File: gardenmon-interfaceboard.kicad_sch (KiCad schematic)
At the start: 0 parts

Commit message: sch: add all connections
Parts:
- added H1, H2, H3, H4: MountingHole, symbol Mechanical:MountingHole
- added J1: Conn_02x20_Odd_Even, symbol Connector_Generic:Conn_02x20_Odd_Even
- added J2, J4, J5: Conn_01x04, symbol Connector_Generic:Conn_01x04
- added J3: Conn_01x10, symbol Connector_Generic:Conn_01x10
- added J6: Conn_01x03, symbol Connector_Generic:Conn_01x03
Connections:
- new net +3.3V: J1.1 (Pin_1), J1.17 (Pin_17)
- new net +3V3: J2.1 (Pin_1), J3.1 (Pin_1), J4.1 (Pin_1), J5.1 (Pin_1), J6.1 (Pin_1)
- new net 1wire_data: J1.7 (Pin_7), J6.2 (Pin_2)
- new net GND: J1.14 (Pin_14), J1.20 (Pin_20), J1.25 (Pin_25), J1.30 (Pin_30), J1.34 (Pin_34), J1.39 (Pin_39), J1.6 (Pin_6), J1.9 (Pin_9), J2.2 (Pin_2), J3.2 (Pin_2), J3.5 (Pin_5), J4.2 (Pin_2), J5.2 (Pin_2), J6.3 (Pin_3)
- new net i2c_scl: J1.5 (Pin_5), J3.3 (Pin_3), J4.3 (Pin_3), J5.3 (Pin_3)
- new net i2c_sda: J1.3 (Pin_3), J3.4 (Pin_4), J4.4 (Pin_4), J5.4 (Pin_4)
- new net smoist_sig: J2.4 (Pin_4), J3.7 (Pin_7)
- no-connect marks 0 -> 32
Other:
- note added: "I2C address 0x23"
- note added: "I2C address 0x40"
- note added: "address pin tied low -> I2C address 0x48"
- note added: "ads1115 ADC"
- note added: "ambient light sensor"
- note added: "ds18b20 temperature sensor module board (module board has built-in pull up for 1wire_data)"
- note added: "raspberry pi zero 2 w header"
- note added: "sht30 temperature/humidity sensor"
- note added: "soil moisture sensor module board"

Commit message: sch/pcb: add footprints, setup PCBNew for OSHPark
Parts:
- H1, H2, H3, H4: footprint (none) -> MountingHole:MountingHole_2.7mm_M2.5
- J1: footprint (none) -> Connector_PinHeader_2.54mm:PinHeader_2x20_P2.54mm_Vertical
- J2, J4, J5: footprint (none) -> Connector_PinHeader_2.54mm:PinHeader_1x04_P2.54mm_Vertical
- J3: footprint (none) -> Connector_PinHeader_2.54mm:PinHeader_1x10_P2.54mm_Vertical
- J6: footprint (none) -> Connector_PinHeader_2.54mm:PinHeader_1x03_P2.54mm_Vertical
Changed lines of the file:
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@@
       (effects (font (size 1.27 1.27)) (justify left) hide)
     )
-    (property "Footprint" "" (at 130.81 59.69 0)
+    (property "Footprint" "Connector_PinHeader_2.54mm:PinHeader_1x04_P2.54mm_Vertical" (at 130.81 59.69 0)
       (effects (font (size 1.27 1.27)) hide)
     )
@@
       (effects (font (size 1.27 1.27)) (justify left) hide)
     )
-    (property "Footprint" "" (at 130.81 91.44 0)
+    (property "Footprint" "Connector_PinHeader_2.54mm:PinHeader_1x04_P2.54mm_Vertical" (at 130.81 91.44 0)
       (effects (font (size 1.27 1.27)) hide)
     )
@@
       (effects (font (size 1.27 1.27)) (justify left) hide)
     )
-    (property "Footprint" "" (at 130.81 123.19 0)
+    (property "Footprint" "Connector_PinHeader_2.54mm:PinHeader_1x04_P2.54mm_Vertical" (at 130.81 123.19 0)
       (effects (font (size 1.27 1.27)) hide)
     )
@@
       (effects (font (size 1.27 1.27)) (justify left))
     )
-    (property "Footprint" "" (at 68.58 149.86 0)
+    (property "Footprint" "MountingHole:MountingHole_2.7mm_M2.5" (at 68.58 149.86 0)
       (effects (font (size 1.27 1.27)) hide)
     )
@@
       (effects (font (size 1.27 1.27)) (justify left))
     )
-    (property "Footprint" "" (at 68.58 144.78 0)
+    (property "Footprint" "MountingHole:MountingHole_2.7mm_M2.5" (at 68.58 144.78 0)
       (effects (font (size 1.27 1.27)) hide)
     )
@@
       (effects (font (size 1.27 1.27)) (justify left) hide)
     )
-    (property "Footprint" "" (at 193.04 124.46 0)
+    (property "Footprint" "Connector_PinHeader_2.54mm:PinHeader_1x03_P2.54mm_Vertical" (at 193.04 124.46 0)
       (effects (font (size 1.27 1.27)) hide)
     )
@@
       (effects (font (size 1.27 1.27)) (justify left))
     )
-    (property "Footprint" "" (at 68.58 160.02 0)
+    (property "Footprint" "MountingHole:MountingHole_2.7mm_M2.5" (at 68.58 160.02 0)
       (effects (font (size 1.27 1.27)) hide)
     )
@@
       (effects (font (size 1.27 1.27)) (justify left) hide)
     )
-    (property "Footprint" "" (at 191.77 67.31 0)
+    (property "Footprint" "Connector_PinHeader_2.54mm:PinHeader_1x10_P2.54mm_Vertical" (at 191.77 67.31 0)
       (effects (font (size 1.27 1.27)) hide)
     )
@@
       (effects (font (size 1.27 1.27)) hide)
     )
-    (property "Footprint" "" (at 76.2 82.55 0)
+    (property "Footprint" "Connector_PinHeader_2.54mm:PinHeader_2x20_P2.54mm_Vertical" (at 76.2 82.55 0)
       (effects (font (size 1.27 1.27)) hide)
     )
@@
       (effects (font (size 1.27 1.27)) (justify left))
     )
-    (property "Footprint" "" (at 68.58 154.94 0)
-      (effects (font (size 1.27 1.27)) hide)
-    )
+    (property "Footprint" "MountingHole:MountingHole_2.7mm_M2.5" (at 68.58 154.94 0)
+      (effects (font (size 1.27 1.27)) hide)
+    )

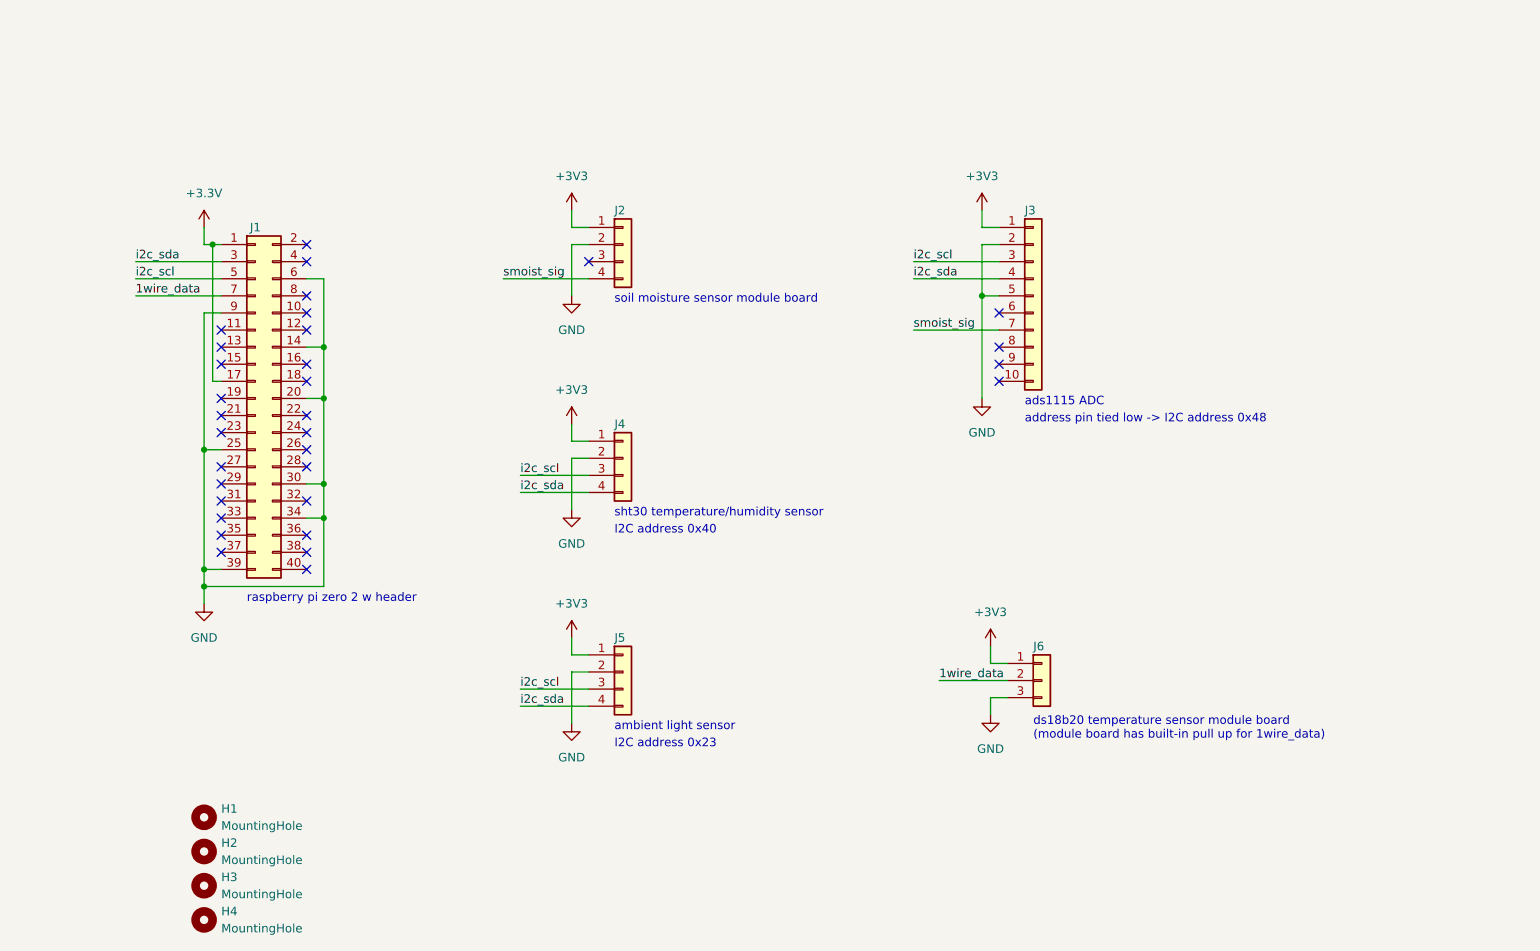
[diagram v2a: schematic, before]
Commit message: pcb: add footprints, board layout
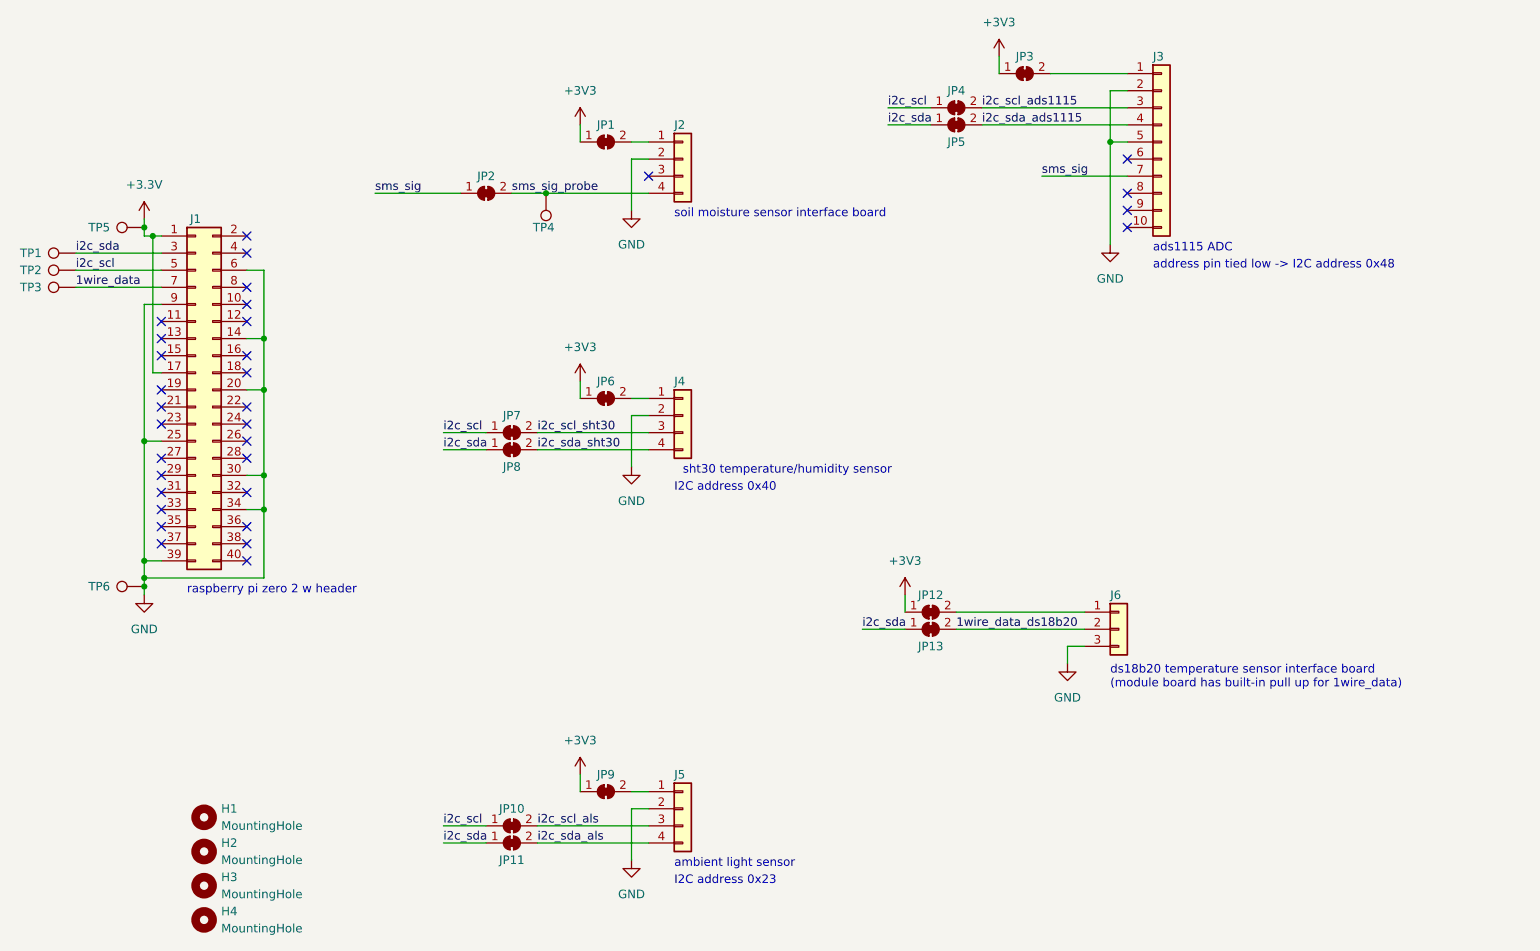
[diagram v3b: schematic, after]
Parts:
- added JP1, JP10, JP11, JP12, JP13, JP2, JP3, JP4, JP5, JP6, JP7, JP8, JP9: SolderJumper_2_Bridged, Jumper:SolderJumper-2_P1.3mm_Open_TrianglePad1.0x1.5mm, symbol Jumper:SolderJumper_2_Bridged
- added TP1, TP2, TP3, TP4, TP5, TP6: TestPoint, TestPoint:TestPoint_THTPad_2.5x2.5mm_Drill1.2mm, symbol Connector:TestPoint
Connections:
- net +3.3V: now also TP5.1
- net +3V3: now also JP1.1 (A), JP12.1 (A), JP3.1 (A), JP6.1 (A), JP9.1 (A); no longer J2.1 (Pin_1), J3.1 (Pin_1), J4.1 (Pin_1), J5.1 (Pin_1), J6.1 (Pin_1)
- net 1wire_data: now also TP3.1; no longer J6.2 (Pin_2)
- net GND: now also TP6.1
- net i2c_scl: now also JP10.1 (A), JP4.1 (A), JP7.1 (A), TP2.1; no longer J3.3 (Pin_3), J4.3 (Pin_3), J5.3 (Pin_3)
- net i2c_sda: now also JP11.1 (A), JP13.1 (A), JP5.1 (A), JP8.1 (A), TP1.1; no longer J3.4 (Pin_4), J4.4 (Pin_4), J5.4 (Pin_4)
- net smoist_sig renamed sms_sig
- net sms_sig: now also JP2.1 (A); no longer J2.4 (Pin_4)
- new net: J2.1 (Pin_1), JP1.2 (B)
- new net: J4.1 (Pin_1), JP6.2 (B)
- new net: J5.1 (Pin_1), JP9.2 (B)
- new net: J3.1 (Pin_1), JP3.2 (B)
- new net: J6.1 (Pin_1), JP12.2 (B)
- new net 1wire_data_ds18b20: J6.2 (Pin_2), JP13.2 (B)
- new net i2c_scl_ads1115: J3.3 (Pin_3), JP4.2 (B)
- new net i2c_scl_als: J5.3 (Pin_3), JP10.2 (B)
- new net i2c_scl_sht30: J4.3 (Pin_3), JP7.2 (B)
- new net i2c_sda_ads1115: J3.4 (Pin_4), JP5.2 (B)
- new net i2c_sda_als: J5.4 (Pin_4), JP11.2 (B)
- new net i2c_sda_sht30: J4.4 (Pin_4), JP8.2 (B)
- new net sms_sig_probe: J2.4 (Pin_4), JP2.2 (B), TP4.1
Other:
- note added: "ds18b20 temperature sensor interface board (module board has built-in pull up for 1wire_data)"
- note added: "soil moisture sensor interface board"
- note removed: "ds18b20 temperature sensor module board (module board has built-in pull up for 1wire_data)"
- note removed: "soil moisture sensor module board"
- moved on the sheet: J1, J2, J3, J4, J5, J6

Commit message: temp:
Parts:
- removed J3: Conn_01x10, Connector_PinHeader_2.54mm:PinHeader_1x10_P2.54mm_Vertical, symbol Connector_Generic:Conn_01x10
- added C1: 10uF, Capacitor_SMD:C_0603_1608Metric_Pad1.08x0.95mm_HandSolder, symbol Device:C_Small
- added C2: 0.1uF, Capacitor_SMD:C_0603_1608Metric_Pad1.08x0.95mm_HandSolder, symbol Device:C_Small
- added R1: 4.7k, Resistor_SMD:R_0603_1608Metric_Pad0.98x0.95mm_HandSolder, symbol Device:R_Small_US
- added U1: MCP3221A5, Package_TO_SOT_SMD:SOT-23-5_HandSoldering, symbol gardenmon-interfaceboard:MCP3221A5
- J2, J4, J5: footprint Connector_PinHeader_2.54mm:PinHeader_1x04_P2.54mm_Vertical -> Connector_PinSocket_2.54mm:PinSocket_1x04_P2.54mm_Vertical
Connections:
- net +3V3: now also JP1.2 (B); no longer JP1.1 (A)
- net 1wire_data: now also JP13.1 (A)
- net 1wire_data_ds18b20: now also R1.2
- net GND: now also C1.2, C2.2, U1.2 (VSS)
- net i2c_sda: no longer JP13.1 (A)
- net at J2.1 (Pin_1): now also JP1.1 (A); no longer JP1.2 (B)
- net at JP3.2 (B): now also C1.1, C2.1, U1.1 (VDD)
- net at J6.1 (Pin_1), JP12.2 (B): now also R1.1
- net i2c_scl_ads1115 renamed i2c_scl_mcp3221
- net i2c_scl_mcp3221: now also U1.5 (SCL)
- net i2c_sda_ads1115 renamed i2c_sda_mcp3221
- net i2c_sda_mcp3221: now also U1.4 (SDA)
- net sms_sig: no longer names the net of JP2.1 (A)
- net sms_sig: now also U1.3 (AIN)
- net sms_sig_probe: no longer names the net of J2.4 (Pin_4), JP2.2 (B), TP4.1
- no-connect marks 32 -> 28
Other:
- note added: "I2C Address: 0x4D"
- note added: "ds18b20 temperature sensor"
- note removed: "address pin tied low -> I2C address 0x48"
- note removed: "ads1115 ADC"
- note removed: "ds18b20 temperature sensor interface board (module board has built-in pull up for 1wire_data)"
- moved on the sheet: J2, JP1, JP12, JP13, JP2, JP3, JP4, JP5, TP4

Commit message: rev0: release of rev0
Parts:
- removed J2: Conn_01x04, Connector_PinSocket_2.54mm:PinSocket_1x04_P2.54mm_Vertical, symbol Connector_Generic:Conn_01x04
- added J4: Conn_01x02, Connector_JST:JST_PH_S2B-PH-K_1x02_P2.00mm_Horizontal, symbol Connector_Generic:Conn_01x02
- added R1: 10k, Resistor_SMD:R_0603_1608Metric_Pad0.98x0.95mm_HandSolder, symbol Device:R_Small_US
- C1: Part Number (none) -> CL10A106KQ8NNNC
- C2: Part Number (none) -> CL10B104KB8NNWC
- J2: renamed from J4; footprint Connector_PinSocket_2.54mm:PinSocket_1x04_P2.54mm_Vertical -> Connector_JST:JST_PH_S4B-PH-K_1x04_P2.00mm_Horizontal; Link (none) -> https://www.digikey.com/en/products/detail/jst-sales-americ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; Part Number (none) -> S4B-PH-K-S
- J3: renamed from J5; footprint Connector_PinSocket_2.54mm:PinSocket_1x04_P2.54mm_Vertical -> Connector_JST:JST_PH_S4B-PH-K_1x04_P2.00mm_Horizontal; Link (none) -> https://www.digikey.com/en/products/detail/jst-sales-americ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; Part Number (none) -> S4B-PH-K-S
- J5: renamed from J6; footprint Connector_PinHeader_2.54mm:PinHeader_1x03_P2.54mm_Vertical -> Connector_JST:JST_PH_S3B-PH-K_1x03_P2.00mm_Horizontal; Link (none) -> https://www.digikey.com/en/products/detail/jst-sales-americ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; Part Number (none) -> S3B-PH-K-S
- R2: renamed from R1; Link (none) -> https://www.digikey.com/en/products/detail/yageo/RC0603FR-0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; Part Number (none) -> RC0603FR-074K7L
- U1: Part Number (none) -> MCP3221A5T-E/OT
- renumbered JP7 to JP1, JP3 to JP10, JP2 to JP11, JP4 to JP12, JP5 to JP13, JP8 to JP2, JP10 to JP3, JP11 to JP4, JP6 to JP5, JP9 to JP6, JP1 to JP7, JP12 to JP8, JP13 to JP9, TP5 to TP4, TP6 to TP5, TP4 to TP6
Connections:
- net +3V3: now also J1.1 (Pin_1), TP4.1
- net GND: now also R1.2
- net at JP7.1 (A): now also J4.1 (Pin_1)
- net at JP11.2 (B), TP6.1: now also J4.2 (Pin_2), R1.1
- removed net +3.3V: J1.1 (Pin_1), J1.17 (Pin_17), TP4.1
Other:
- note added: "Ambient Light Sensor (ALS) I2C address 0x23"
- note added: "Soil Moisture Sensor (SMS)"
- note added: "ds18b20 temperature sensor Soil Temperature Sensor (STS)"
- note added: "sht30 temperature/humidity sensor Ambient Temperature/Humidity Sensor (ATHS) I2C address 0x40"
- note removed: "I2C address 0x23"
- note removed: "I2C address 0x40"
- note removed: "ambient light sensor"
- note removed: "ds18b20 temperature sensor"
- note removed: "sht30 temperature/humidity sensor"
- note removed: "soil moisture sensor interface board"
- moved on the sheet: C1, C2, J2, J3, J5, JP1, JP10, JP11, JP12, JP13, JP2, JP3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
